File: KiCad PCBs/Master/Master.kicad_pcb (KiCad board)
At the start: 2 copper layers, 79.4 x 55.2 mm, 17 parts

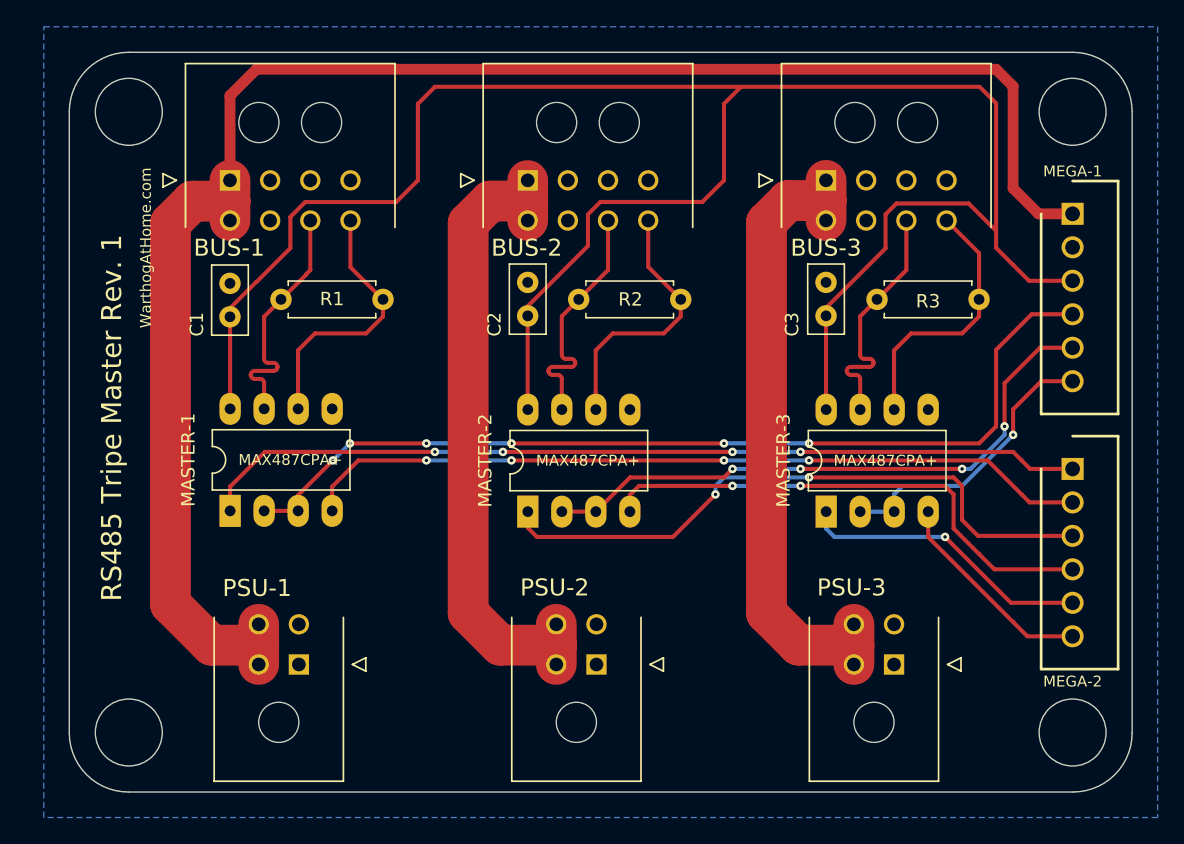
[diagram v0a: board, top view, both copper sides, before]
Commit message: Fixed mounting holes Added Mega pin labels
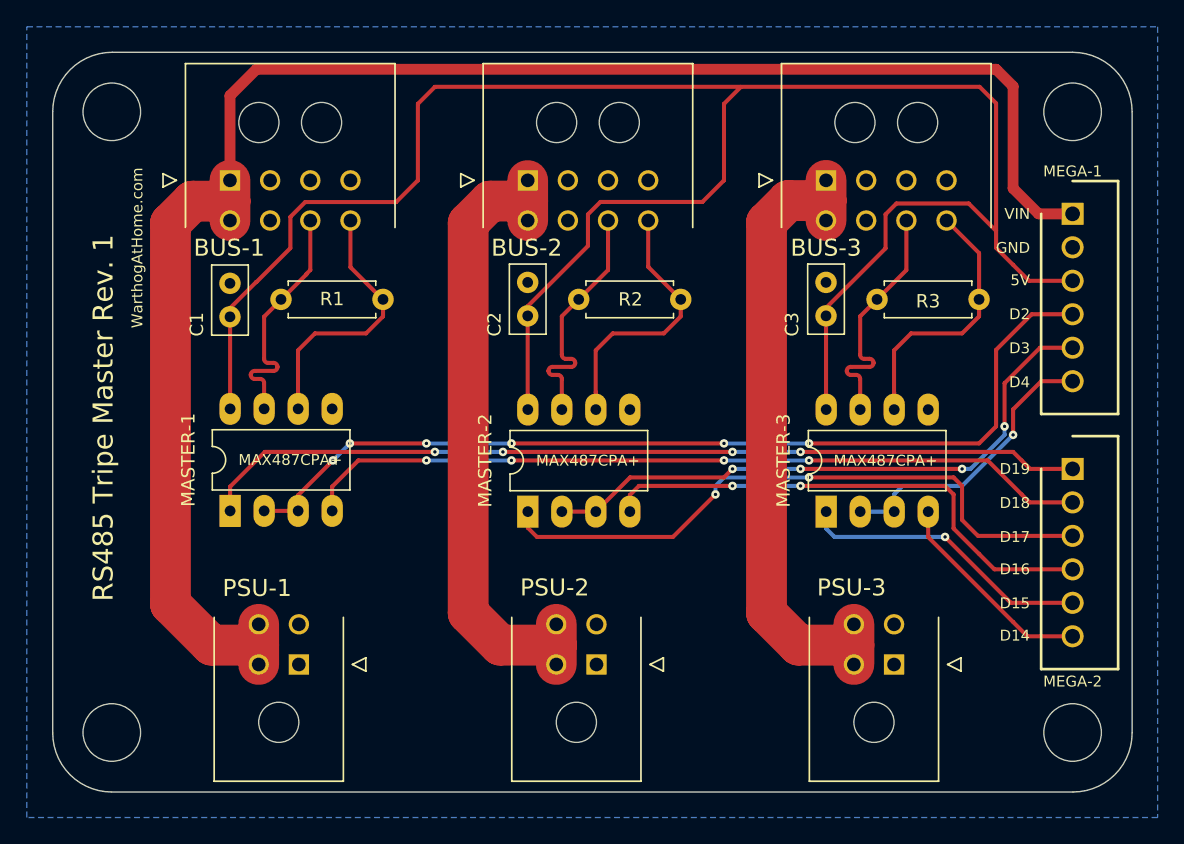
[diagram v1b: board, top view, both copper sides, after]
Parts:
- added REF**: MountingHole_4.3mm_M4, MountingHole:MountingHole_4.3mm_M4, F.Cu at (99.7, 26.7)
- added REF**: MountingHole_4.3mm_M4, MountingHole:MountingHole_4.3mm_M4, F.Cu at (99.7, 73.0)
- added REF**: MountingHole_4.3mm_M4, MountingHole:MountingHole_4.3mm_M4, F.Cu at (27.9, 26.7)
- added REF**: MountingHole_4.3mm_M4, MountingHole:MountingHole_4.3mm_M4, F.Cu at (27.9, 73.0)
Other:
- board size 79.4 x 55.2 mm -> 80.6 x 55.2 mm
- board text added: "5V"
- board text added: "D14"
- board text added: "D15"
- board text added: "D16"
- board text added: "D17"
- board text added: "D18"
- board text added: "D19"
- board text added: "D2"
- board text added: "D3"
- board text added: "D4"
- board text added: "GND"
- board text added: "VIN"
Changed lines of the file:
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@@
   (net 25 "unconnected-(BUS-3-Pad3)")
   (net 26 "unconnected-(BUS-3-Pad4)")
+  (footprint "MountingHole:MountingHole_4.3mm_M4" (layer "F.Cu")
+    (at 99.695 26.67)
+    (descr "Mounting Hole 4.3mm, no annular, M4")
+    (tags "mounting hole 4.3mm no annular m4")
+    (attr board_only exclude_from_pos_files exclude_from_bom)
+    (fp_text reference "REF**" (at 0 -5.3) (layer "F.SilkS") hide
+      (effects (font (size 1 1) (thickness 0.15)))
+    )
+    (fp_text value "MountingHole_4.3mm_M4" (at 0 5.3) (layer "F.Fab") hide
+      (effects (font (size 1 1) (thickness 0.15)))
+    )
+    (fp_text user "${REFERENCE}" (at 0 0) (layer "F.Fab") hide
+      (effects (font (size 1 1) (thickness 0.15)))
+    )
+    (fp_circle (center 0 0) (end 4.3 0) (layer "Cmts.User") (width 0.15) (fill none))
+    (fp_circle (center 0 0) (end 4.55 0) (layer "F.CrtYd") (width 0.05) (fill none))
+    (pad "" np_thru_hole circle (at 0 0) (size 4.3 4.3) (drill 4.3) (layers *.Cu *.Mask))
+  )
   (footprint "Capacitor_THT:C_Disc_D5.0mm_W2.5mm_P2.50mm" (layer "F.Cu")
     (at 59 39.41 -90)
@@
       (rotate (xyz 0 0 0))
     )
+  )
+  (footprint "MountingHole:MountingHole_4.3mm_M4" (layer "F.Cu")
+    (at 99.695 73.025)
+    (descr "Mounting Hole 4.3mm, no annular, M4")
+    (tags "mounting hole 4.3mm no annular m4")
+    (attr board_only exclude_from_pos_files exclude_from_bom)
+    (fp_text reference "REF**" (at 0 -5.3) (layer "F.SilkS") hide
+      (effects (font (size 1 1) (thickness 0.15)))
+    )
+    (fp_text value "MountingHole_4.3mm_M4" (at 0 5.3) (layer "F.Fab") hide
+      (effects (font (size 1 1) (thickness 0.15)))
+    )
+    (fp_text user "${REFERENCE}" (at 0 0) (layer "F.Fab") hide
+      (effects (font (size 1 1) (thickness 0.15)))
+    )
+    (fp_circle (center 0 0) (end 4.3 0) (layer "Cmts.User") (width 0.15) (fill none))
+    (fp_circle (center 0 0) (end 4.55 0) (layer "F.CrtYd") (width 0.05) (fill none))
+    (pad "" np_thru_hole circle (at 0 0) (size 4.3 4.3) (drill 4.3) (layers *.Cu *.Mask))
   )
   (footprint "A10 KiCad Libraries:SHDR6W64P0X250_1X6_1740X575X700P" (layer "F.Cu")
@@
       (rotate (xyz 0 0 0))
     )
+  )
+  (footprint "MountingHole:MountingHole_4.3mm_M4" (layer "F.Cu")
+    (at 27.94 26.67)
+    (descr "Mounting Hole 4.3mm, no annular, M4")
+    (tags "mounting hole 4.3mm no annular m4")
+    (attr board_only exclude_from_pos_files exclude_from_bom)
+    (fp_text reference "REF**" (at 0 -5.3) (layer "F.SilkS") hide
+      (effects (font (size 1 1) (thickness 0.15)))
+    )
+    (fp_text value "MountingHole_4.3mm_M4" (at 0 5.3) (layer "F.Fab") hide
+      (effects (font (size 1 1) (thickness 0.15)))
+    )
+    (fp_text user "${REFERENCE}" (at 0 0) (layer "F.Fab") hide
+      (effects (font (size 1 1) (thickness 0.15)))
+    )
+    (fp_circle (center 0 0) (end 4.3 0) (layer "Cmts.User") (width 0.15) (fill none))
+    (fp_circle (center 0 0) (end 4.55 0) (layer "F.CrtYd") (width 0.05) (fill none))
+    (pad "" np_thru_hole circle (at 0 0) (size 4.3 4.3) (drill 4.3) (layers *.Cu *.Mask))
   )
   (footprint "A10 KiCad Libraries:Molex 43045-0800" (layer "F.Cu")
@@
     )
   )
+  (footprint "MountingHole:MountingHole_4.3mm_M4" (layer "F.Cu")
+    (at 27.94 73.025)
+    (descr "Mounting Hole 4.3mm, no annular, M4")
+    (tags "mounting hole 4.3mm no annular m4")
+    (attr board_only exclude_from_pos_files exclude_from_bom)
+    (fp_text reference "REF**" (at 0 -5.3) (layer "F.SilkS") hide
+      (effects (font (size 1 1) (thickness 0.15)))
+    )
+    (fp_text value "MountingHole_4.3mm_M4" (at 0 5.3) (layer "F.Fab") hide
+      (effects (font (size 1 1) (thickness 0.15)))
+    )
+    (fp_text user "${REFERENCE}" (at 0 0) (layer "F.Fab") hide
+      (effects (font (size 1 1) (thickness 0.15)))
+    )
+    (fp_circle (center 0 0) (end 4.3 0) (layer "Cmts.User") (width 0.15) (fill none))
+    (fp_circle (center 0 0) (end 4.55 0) (layer "F.CrtYd") (width 0.05) (fill none))
+    (pad "" np_thru_hole circle (at 0 0) (size 4.3 4.3) (drill 4.3) (layers *.Cu *.Mask))
+  )
   (footprint "Capacitor_THT:C_Disc_D5.0mm_W2.5mm_P2.50mm" (layer "F.Cu")
     (at 81.28 39.41 -90)
@@
     )
   )
-  (gr_line (start 24.765 73.05691) (end 24.765 26.67) (layer "Edge.Cuts") (width 0.1))
+  (gr_line (start 23.52691 73.05691) (end 23.52691 26.67) (layer "Edge.Cuts") (width 0.1))
   (gr_arc (start 104.14 73.05691) (mid 102.847436 76.177436) (end 99.72691 77.47) (layer "Edge.Cuts") (width 0.1016))
-  (gr_arc (start 29.17809 77.47) (mid 26.057564 76.177436) (end 24.765 73.05691) (layer "Edge.Cuts") (width 0.1016))
+  (gr_arc (start 27.94 77.47) (mid 24.819474 76.177436) (end 23.52691 73.05691) (layer "Edge.Cuts") (width 0.1016))
   (gr_arc (start 99.695 22.225) (mid 102.83809 23.52691) (end 104.14 26.67) (layer "Edge.Cuts") (width 0.1016))
-  (gr_circle (center 99.695 73.025) (end 102.195 73.025) (layer "Edge.Cuts") (width 0.1) (fill none))
-  (gr_circle (center 29.21 73.025) (end 31.71 73.025) (layer "Edge.Cuts") (width 0.1) (fill none))
-  (gr_circle (center 29.21 26.67) (end 31.71 26.67) (layer "Edge.Cuts") (width 0.1) (fill none))
-  (gr_circle (center 99.695 26.67) (end 102.195 26.67) (layer "Edge.Cuts") (width 0.1) (fill none))
-  (gr_line (start 99.72691 77.47) (end 29.17809 77.47) (layer "Edge.Cuts") (width 0.1))
+  (gr_line (start 99.72691 77.47) (end 27.94 77.47) (layer "Edge.Cuts") (width 0.1))
   (gr_line (start 104.14 26.67) (end 104.14 73.05691) (layer "Edge.Cuts") (width 0.1))
-  (gr_arc (start 24.765 26.67) (mid 26.06691 23.52691) (end 29.21 22.225) (layer "Edge.Cuts") (width 0.1016))
-  (gr_line (start 29.21 22.225) (end 99.695 22.225) (layer "Edge.Cuts") (width 0.1))
+  (gr_arc (start 23.52691 26.67) (mid 24.82882 23.52691) (end 27.97191 22.225) (layer "Edge.Cuts") (width 0.1016))
+  (gr_line (start 27.97191 22.225) (end 99.695 22.225) (layer "Edge.Cuts") (width 0.1))
   (gr_text "BRRRRRRRRRRT" (at 64.135 49.53 15) (layer "B.SilkS")
     (effects (font (size 5.842 5.842) (thickness 1.2192)) (justify mirror))
   )
-  (gr_text "WarthogAtHome.com" (at 30.48 36.83 90) (layer "F.SilkS")
+  (gr_text "D14" (at 96.52 65.786) (layer "F.SilkS")
+    (effects (font (size 0.8128 0.8128) (thickness 0.1524)) (justify right))
+  )
+  (gr_text "GND" (at 96.52 36.83) (layer "F.SilkS")
+    (effects (font (size 0.8128 0.8128) (thickness 0.1524)) (justify right))
+  )
+  (gr_text "D15" (at 96.52 63.373) (layer "F.SilkS")
+    (effects (font (size 0.8128 0.8128) (thickness 0.1524)) (justify right))
+  )
+  (gr_text "D4" (at 96.52 46.863) (layer "F.SilkS")
+    (effects (font (size 0.8128 0.8128) (thickness 0.1524)) (justify right))
+  )
+  (gr_text "5V" (at 96.52 39.243) (layer "F.SilkS")
+    (effects (font (size 0.8128 0.8128) (thickness 0.1524)) (justify right))
+  )
+  (gr_text "D3" (at 96.52 44.323) (layer "F.SilkS")
+    (effects (font (size 0.8128 0.8128) (thickness 0.1524)) (justify right))
+  )
+  (gr_text "D16" (at 96.52 60.833) (layer "F.SilkS")
+    (effects (font (size 0.8128 0.8128) (thickness 0.1524)) (justify right))
+  )
+  (gr_text "WarthogAtHome.com" (at 29.845 36.83 90) (layer "F.SilkS")
     (effects (font (size 0.8128 0.8128) (thickness 0.2032)))
   )
-  (gr_text "RS485 Tripe Master Rev. 1" (at 27.94 49.53 90) (layer "F.SilkS")
+  (gr_text "D18" (at 96.52 55.88) (layer "F.SilkS")
+    (effects (font (size 0.8128 0.8128) (thickness 0.1524)) (justify right))
+  )
+  (gr_text "D19" (at 96.52 53.34) (layer "F.SilkS")
+    (effects (font (size 0.8128 0.8128) (thickness 0.1524)) (justify right))
+  )
+  (gr_text "D17" (at 96.52 58.42) (layer "F.SilkS")
+    (effects (font (size 0.8128 0.8128) (thickness 0.1524)) (justify right))
+  )
+  (gr_text "D2" (at 96.52 41.783) (layer "F.SilkS")
+    (effects (font (size 0.8128 0.8128) (thickness 0.1524)) (justify right))
+  )
+  (gr_text "RS485 Tripe Master Rev. 1" (at 27.305 49.53 90) (layer "F.SilkS")
     (effects (font (size 1.5 1.5) (thickness 0.3)))
+  )
+  (gr_text "VIN" (at 96.52 34.29) (layer "F.SilkS")
+    (effects (font (size 0.8128 0.8128) (thickness 0.1524)) (justify right))
   )
   (segment (start 74.295 52.07) (end 57.15 52.07) (width 0.3048) (layer "F.Cu") (net 3))
@@
       (pts
         (xy 106.045 79.375)
-        (xy 22.86 79.375)
-        (xy 22.86 20.32)
+        (xy 21.59 79.375)
+        (xy 21.59 20.32)
         (xy 106.045 20.32)
       )

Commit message: Added a ground pour to top layer
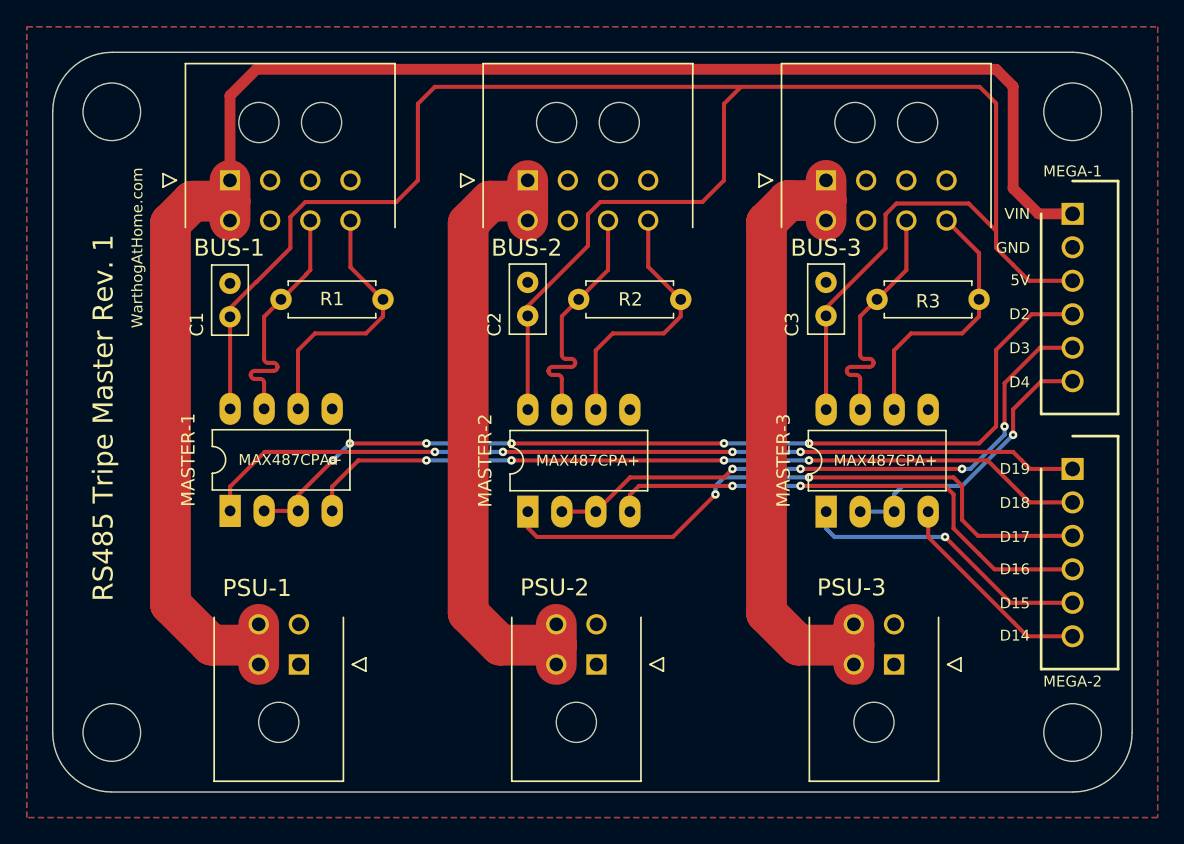
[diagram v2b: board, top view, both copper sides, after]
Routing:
- added copper zone on F.Cu, net GND
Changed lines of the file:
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@@
   (segment (start 92.71 37.22) (end 90.28 34.79) (width 0.3048) (layer "F.Cu") (net 22))
   (segment (start 91.44 43.22) (end 92.71 41.95) (width 0.3048) (layer "F.Cu") (net 22))
+  (zone (net 11) (net_name "GND") (layer "F.Cu") (name "GND") (hatch edge 0.508)
+    (connect_pads (clearance 0.6096))
+    (min_thickness 0.2032) (filled_areas_thickness no)
+    (fill yes (thermal_gap 0.6096) (thermal_bridge_width 0.8128) (smoothing chamfer) (radius 0.8128))
+    (polygon
+      (pts
+        (xy 106.045 79.375)
+        (xy 21.59 79.375)
+        (xy 21.59 20.32)
+        (xy 106.045 20.32)
+      )
+    )
+  )
   (zone (net 11) (net_name "GND") (layer "B.Cu") (name "GND") (hatch edge 0.508)
     (connect_pads (clearance 0.6096))
